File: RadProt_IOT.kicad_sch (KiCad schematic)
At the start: 10 parts, among them J1 Conn_01x04_Pin, J2 Conn_01x04_Pin, J3 Conn_01x04_Pin, J4 OUT+, J5 OUT-, J6 Conn_02x05_Top_Bottom, SW1 Config

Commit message: manually routed, 1 route needs bridge
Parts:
- J4, J5: footprint Connector_PinHeader_2.54mm:PinHeader_1x01_P2.54mm_Horizontal -> Connector_PinHeader_2.54mm:PinHeader_1x01_P2.54mm_Vertical
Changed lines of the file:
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@@
 			)
 		)
-		(property "Footprint" "Connector_PinHeader_2.54mm:PinHeader_1x01_P2.54mm_Horizontal"
+		(property "Footprint" "Connector_PinHeader_2.54mm:PinHeader_1x01_P2.54mm_Vertical"
 			(at 71.12 24.13 0)
 			(effects
@@
 			)
 		)
-		(property "Footprint" "Connector_PinHeader_2.54mm:PinHeader_1x01_P2.54mm_Horizontal"
+		(property "Footprint" "Connector_PinHeader_2.54mm:PinHeader_1x01_P2.54mm_Vertical"
 			(at 71.12 39.37 0)
 			(effects

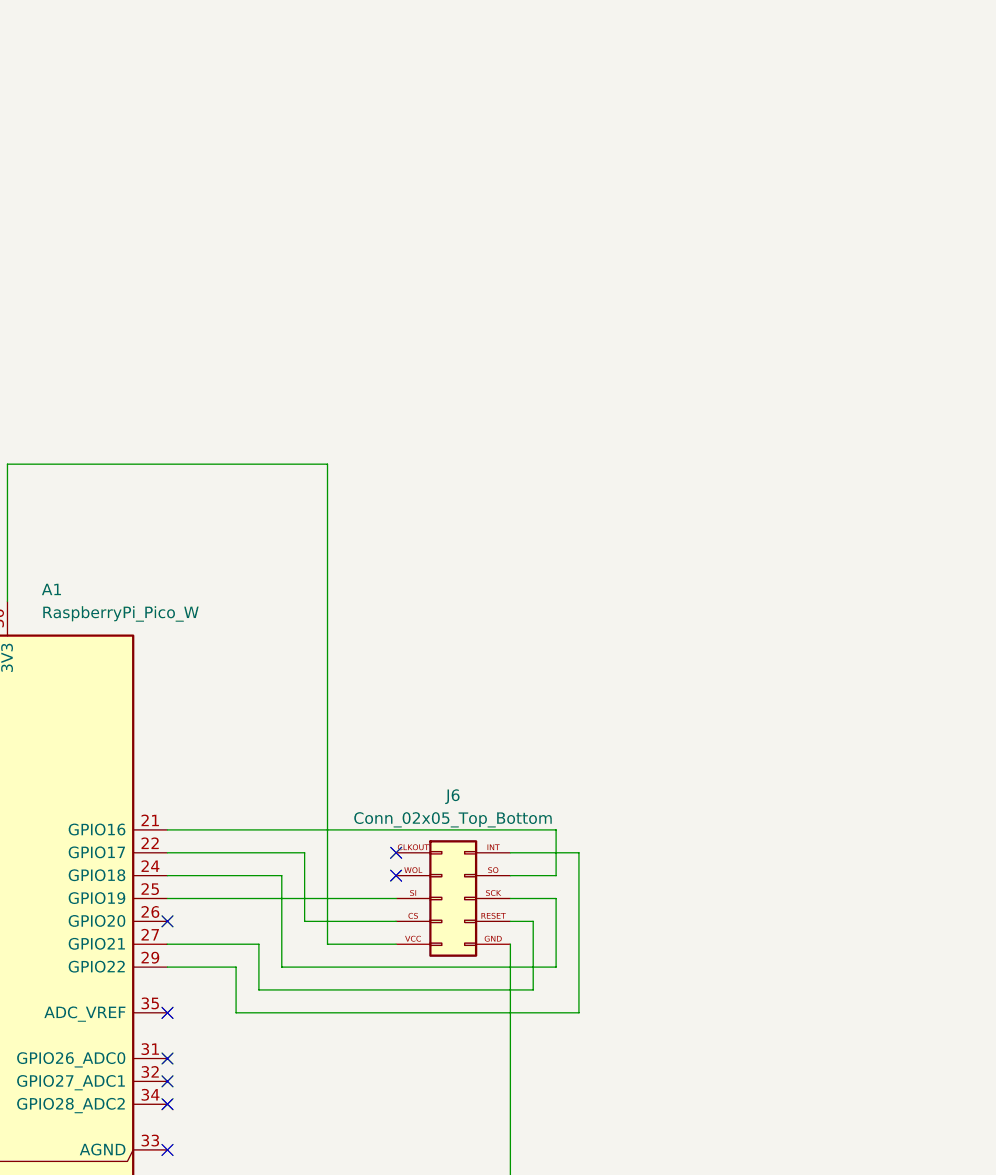
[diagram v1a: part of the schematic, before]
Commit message: routed with 1mm
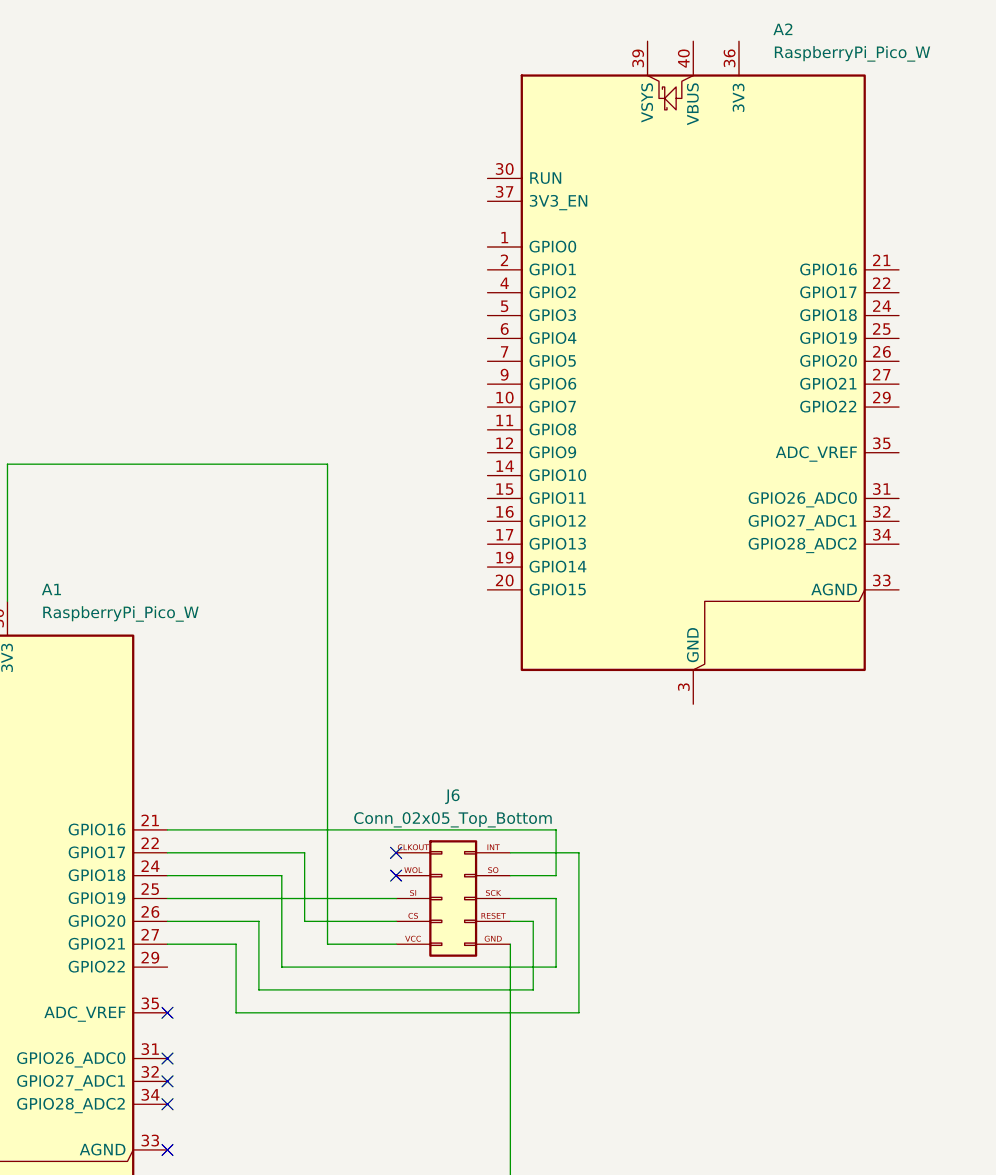
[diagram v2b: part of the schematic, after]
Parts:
- added A2: RaspberryPi_Pico_W, Module:RaspberryPi_Pico_W_SMD_HandSolder, symbol MCU_Module:RaspberryPi_Pico_W
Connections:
- net at A1.26 (GPIO20): now also J6.RESET
- net at A1.27 (GPIO21): now also J6.INT; no longer J6.RESET
- net at A1.29 (GPIO22): no longer J6.INT
- new net: A2.13 (GND), A2.18 (GND), A2.23 (GND), A2.28 (GND), A2.3 (GND), A2.38 (GND), A2.8 (GND)
- no-connect marks 25 -> 24
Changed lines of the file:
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@@
 	)
 	(no_connect
-		(at 184.15 111.76)
-	)
-	(no_connect
 		(at 184.15 129.54)
 	)
@@
 	(wire
 		(pts
-			(xy 184.15 114.3) (xy 194.31 114.3)
+			(xy 184.15 114.3) (xy 191.77 114.3)
 		)
 		(stroke
@@
 	(wire
 		(pts
-			(xy 184.15 116.84) (xy 191.77 116.84)
-		)
-		(stroke
-			(width 0)
-			(type default)
-		)
-	)
-	(wire
-		(pts
 			(xy 81.28 154.94) (xy 111.76 154.94)
 		)
@@
 	(wire
 		(pts
+			(xy 184.15 111.76) (xy 194.31 111.76)
+		)
+		(stroke
+			(width 0)
+			(type default)
+		)
+	)
+	(wire
+		(pts
 			(xy 166.37 60.96) (xy 166.37 76.2)
 		)
@@
 	(wire
 		(pts
-			(xy 194.31 114.3) (xy 194.31 119.38)
+			(xy 194.31 111.76) (xy 194.31 119.38)
 		)
 		(stroke
@@
 	(wire
 		(pts
-			(xy 191.77 116.84) (xy 191.77 121.92)
+			(xy 76.2 149.86) (xy 91.44 149.86)
 		)
 		(stroke
@@
 	(wire
 		(pts
-			(xy 76.2 149.86) (xy 91.44 149.86)
+			(xy 111.76 154.94) (xy 128.27 154.94)
 		)
 		(stroke
@@
 	(wire
 		(pts
-			(xy 111.76 154.94) (xy 128.27 154.94)
+			(xy 128.27 153.67) (xy 128.27 154.94)
 		)
 		(stroke
@@
 	(wire
 		(pts
-			(xy 128.27 153.67) (xy 128.27 154.94)
+			(xy 222.25 154.94) (xy 161.29 154.94)
 		)
 		(stroke
@@
 	(wire
 		(pts
-			(xy 222.25 154.94) (xy 161.29 154.94)
+			(xy 191.77 114.3) (xy 191.77 121.92)
 		)
 		(stroke
@@
 					(unit 1)
 				)
+			)
+		)
+	)
+	(symbol
+		(lib_id "MCU_Module:RaspberryPi_Pico_W")
+		(at 242.57 52.07 0)
+		(unit 1)
+		(exclude_from_sim no)
+		(in_bom yes)
+		(on_board yes)
+		(dnp no)
+		(property "Reference" "A2"
+			(at 251.46 12.7 0)
+			(effects
+				(font
+					(size 1.27 1.27)
+				)
+				(justify left)
+			)
+		)
+		(property "Value" "RaspberryPi_Pico_W"
+			(at 251.46 15.24 0)
+			(effects
+				(font
+					(size 1.27 1.27)
+				)
+				(justify left)
+			)
+		)
+		(property "Footprint" "Module:RaspberryPi_Pico_W_SMD_HandSolder"
+			(at 242.57 99.06 0)
+			(effects
+				(font
+					(size 1.27 1.27)
+				)
+				(hide yes)
+			)
+		)
+		(property "Datasheet" "https://datasheets.raspberrypi.com/picow/pico-w-datasheet.pdf"
+			(at 242.57 101.6 0)
+			(effects
+				(font
+					(size 1.27 1.27)
+				)
+				(hide yes)
+			)
+		)
+		(property "Description" "Versatile and inexpensive wireless microcontroller module powered by RP2040 dual-core Arm Cortex-M0+ processor up to 133 MHz, 264kB SRAM, 2MB QSPI flash, Infineon CYW43439 2.4GHz 802.11n wireless LAN; also supports Raspberry Pi Pico 2 W"
+			(at 242.57 104.14 0)
+			(effects
+				(font
+					(size 1.27 1.27)
+				)
+				(hide yes)
+			)
+		)
+		(pin "34"
+		)
+		(pin "33"
+		)
+		(pin "8"
+		)
+		(pin "24"
+		)
+		(pin "16"
+		)
+		(pin "36"
+		)
+		(pin "17"
+		)
+		(pin "37"
+		)
+		(pin "19"
+		)
+		(pin "12"
+		)
+		(pin "29"
+		)
+		(pin "2"
+		)
+		(pin "1"
+		)
+		(pin "30"
+		)
+		(pin "20"
+		)
+		(pin "40"
+		)
+		(pin "28"
+		)
+		(pin "7"
+		)
+		(pin "22"
+		)
+		(pin "32"
+		)
+		(pin "21"
+		)
+		(pin "4"
+		)
+		(pin "39"
+		)
+		(pin "25"
+		)
+		(pin "26"
+		)
+		(pin "5"
+		)
+		(pin "9"
+		)
+		(pin "3"
+		)
+		(pin "13"
+		)
+		(pin "10"
+		)
+		(pin "23"
+		)
+		(pin "27"
+		)
+		(pin "38"
+		)
+		(pin "18"
+		)
+		(pin "6"
+		)
+		(pin "11"
+		)
+		(pin "15"
+		)
+		(pin "14"
+		)
+		(pin "35"
+		)
+		(pin "31"
+		)
+		(instances
+			(project "RadProt_IOT"
+				(path "/cff4cc2a-e2ab-4a74-8ae5-5e001e0fb180"
+					(reference "A2")
+					(unit 1)
+				)

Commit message: nice
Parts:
- removed A2: RaspberryPi_Pico_W, Module:RaspberryPi_Pico_W_SMD_HandSolder, symbol MCU_Module:RaspberryPi_Pico_W
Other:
- moved on the sheet: SW1
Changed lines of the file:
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@@
 	(wire
 		(pts
-			(xy 111.76 147.32) (xy 111.76 154.94)
+			(xy 199.39 111.76) (xy 209.55 111.76)
 		)
 		(stroke
@@
 	(wire
 		(pts
-			(xy 199.39 111.76) (xy 209.55 111.76)
+			(xy 91.44 101.6) (xy 138.43 101.6)
 		)
 		(stroke
@@
 	(wire
 		(pts
-			(xy 91.44 101.6) (xy 138.43 101.6)
+			(xy 184.15 104.14) (xy 199.39 104.14)
 		)
 		(stroke
@@
 	(wire
 		(pts
-			(xy 184.15 104.14) (xy 199.39 104.14)
+			(xy 224.79 111.76) (xy 222.25 111.76)
 		)
 		(stroke
@@
 	(wire
 		(pts
-			(xy 224.79 111.76) (xy 222.25 111.76)
+			(xy 111.76 154.94) (xy 128.27 154.94)
 		)
 		(stroke
@@
 	(wire
 		(pts
+			(xy 111.76 149.86) (xy 111.76 154.94)
+		)
+		(stroke
+			(width 0)
+			(type default)
+		)
+	)
+	(wire
+		(pts
 			(xy 128.27 144.78) (xy 128.27 146.05)
 		)
@@
 	(wire
 		(pts
-			(xy 111.76 134.62) (xy 111.76 137.16)
+			(xy 111.76 134.62) (xy 111.76 139.7)
 		)
 		(stroke
@@
 	(wire
 		(pts
-			(xy 111.76 154.94) (xy 128.27 154.94)
-		)
-		(stroke
-			(width 0)
-			(type default)
-		)
-	)
-	(wire
-		(pts
 			(xy 128.27 153.67) (xy 128.27 154.94)
 		)
@@
 	)
 	(symbol
-		(lib_id "MCU_Module:RaspberryPi_Pico_W")
-		(at 242.57 52.07 0)
-		(unit 1)
-		(exclude_from_sim no)
-		(in_bom yes)
-		(on_board yes)
-		(dnp no)
-		(property "Reference" "A2"
-			(at 251.46 12.7 0)
-			(effects
-				(font
-					(size 1.27 1.27)
-				)
-				(justify left)
-			)
-		)
-		(property "Value" "RaspberryPi_Pico_W"
-			(at 251.46 15.24 0)
-			(effects
-				(font
-					(size 1.27 1.27)
-				)
-				(justify left)
-			)
-		)
-		(property "Footprint" "Module:RaspberryPi_Pico_W_SMD_HandSolder"
-			(at 242.57 99.06 0)
-			(effects
-				(font
-					(size 1.27 1.27)
-				)
-				(hide yes)
-			)
-		)
-		(property "Datasheet" "https://datasheets.raspberrypi.com/picow/pico-w-datasheet.pdf"
-			(at 242.57 101.6 0)
-			(effects
-				(font
-					(size 1.27 1.27)
-				)
-				(hide yes)
-			)
-		)
-		(property "Description" "Versatile and inexpensive wireless microcontroller module powered by RP2040 dual-core Arm Cortex-M0+ processor up to 133 MHz, 264kB SRAM, 2MB QSPI flash, Infineon CYW43439 2.4GHz 802.11n wireless LAN; also supports Raspberry Pi Pico 2 W"
-			(at 242.57 104.14 0)
-			(effects
-				(font
-					(size 1.27 1.27)
-				)
-				(hide yes)
-			)
-		)
-		(pin "34"
-		)
-		(pin "33"
-		)
-		(pin "8"
-		)
-		(pin "24"
-		)
-		(pin "16"
-		)
-		(pin "36"
-		)
-		(pin "17"
-		)
-		(pin "37"
-		)
-		(pin "19"
-		)
-		(pin "12"
-		)
-		(pin "29"
-		)
-		(pin "2"
-		)
-		(pin "1"
-		)
-		(pin "30"
-		)
-		(pin "20"
-		)
-		(pin "40"
-		)
-		(pin "28"
-		)
-		(pin "7"
-		)
-		(pin "22"
-		)
-		(pin "32"
-		)
-		(pin "21"
-		)
-		(pin "4"
-		)
-		(pin "39"
-		)
-		(pin "25"
-		)
-		(pin "26"
-		)
-		(pin "5"
-		)
-		(pin "9"
-		)
-		(pin "3"
-		)
-		(pin "13"
-		)
-		(pin "10"
-		)
-		(pin "23"
-		)
-		(pin "27"
-		)
-		(pin "38"
-		)
-		(pin "18"
-		)
-		(pin "6"
-		)
-		(pin "11"
-		)
-		(pin "15"
-		)
-		(pin "14"
-		)
-		(pin "35"
-		)
-		(pin "31"
-		)
-		(instances
-			(project "RadProt_IOT"
-				(path "/cff4cc2a-e2ab-4a74-8ae5-5e001e0fb180"
-					(reference "A2")
-					(unit 1)
-				)
-			)
-		)
-	)
-	(symbol
 		(lib_id "Connector:Conn_01x04_Pin")
 		(at 71.12 149.86 0)
@@
 	(symbol
 		(lib_id "Switch:SW_Push")
-		(at 111.76 142.24 90)
+		(at 111.76 144.78 90)
 		(unit 1)
 		(exclude_from_sim no)
@@
 		(fields_autoplaced yes)
 		(property "Reference" "SW1"
-			(at 113.03 140.9699 90)
+			(at 113.03 143.5099 90)
 			(effects
 				(font
@@
 		)
 		(property "Value" "Config"
-			(at 113.03 143.5099 90)
+			(at 113.03 146.0499 90)
 			(effects
 				(font
@@
 		)
 		(property "Footprint" "Button_Switch_THT:SW_PUSH_6mm"
-			(at 106.68 142.24 0)
+			(at 106.68 144.78 0)
 			(effects
 				(font
@@
 		)
 		(property "Datasheet" "~"
-			(at 106.68 142.24 0)
+			(at 106.68 144.78 0)
 			(effects
 				(font
@@
 		)
 		(property "Description" "Push button switch, generic, two pins"
-			(at 111.76 142.24 0)
+			(at 111.76 144.78 0)
 			(effects
 				(font

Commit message: nicer
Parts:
- R1: footprint Resistor_THT:R_Axial_DIN0204_L3.6mm_D1.6mm_P2.54mm_Vertical -> Resistor_THT:R_Axial_DIN0204_L3.6mm_D1.6mm_P5.08mm_Horizontal
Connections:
- net GND: now also D1.1 (K); no longer R1.2
- net at A1.20 (GPIO15): now also R1.1; no longer D1.2 (A)
- new net: D1.2 (A), R1.2
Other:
- moved on the sheet: D1, R1

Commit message: nicer +10
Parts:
- D1: value STATUS -> Status
- renumbered A1 to U1
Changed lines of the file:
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@@
 	)
 	(no_connect
+		(at 76.2 66.04)
+	)
+	(no_connect
 		(at 209.55 106.68)
 	)
@@
 	)
 	(no_connect
-		(at 76.2 66.04)
-	)
-	(no_connect
 		(at 138.43 93.98)
 	)
@@
 		(on_board yes)
 		(dnp no)
-		(property "Reference" "A1"
+		(property "Reference" "U1"
 			(at 170.18 74.93 0)
 			(effects
@@
 			(project ""
 				(path "/cff4cc2a-e2ab-4a74-8ae5-5e001e0fb180"
-					(reference "A1")
+					(reference "U1")
 					(unit 1)
 				)
@@
 			)
 		)
-		(property "Value" "STATUS"
+		(property "Value" "Status"
 			(at 132.08 152.7174 90)
 			(effects
